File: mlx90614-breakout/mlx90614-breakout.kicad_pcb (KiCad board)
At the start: 2 copper layers, 12.7 x 25.4 mm, 8 parts, among them J1 Conn_01x04_Male, U1 MLX90614

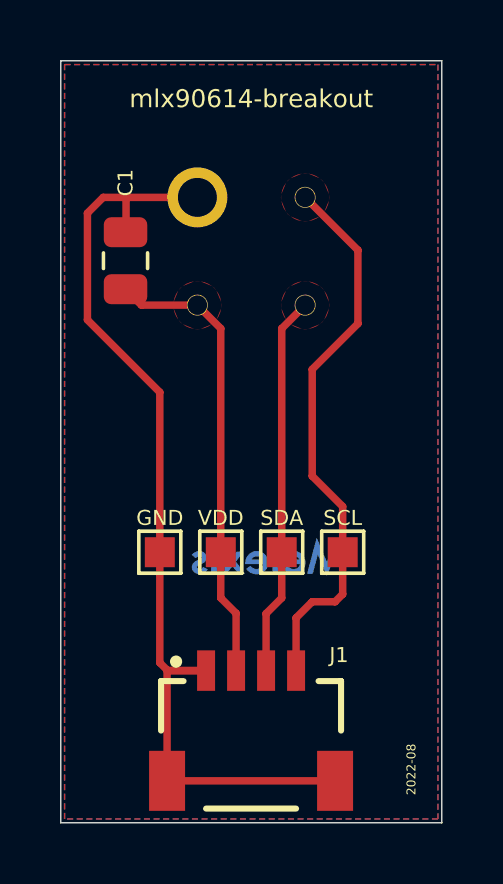
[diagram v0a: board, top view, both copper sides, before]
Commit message: updated breakout boards
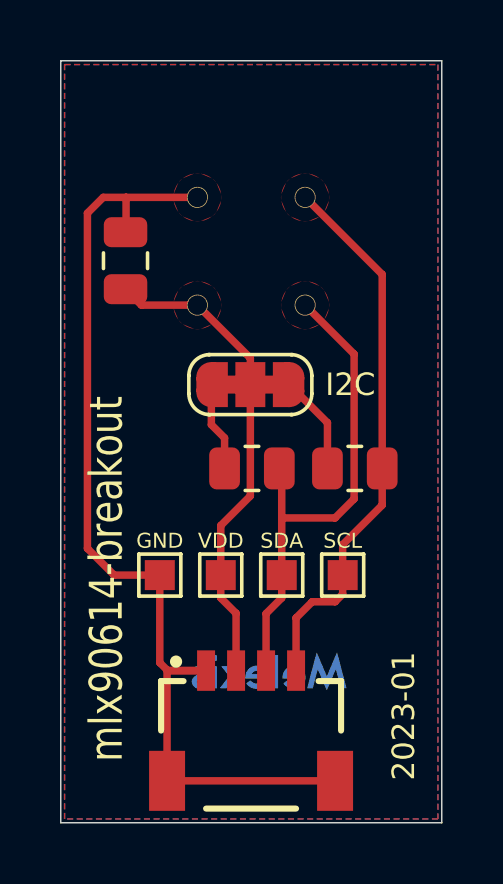
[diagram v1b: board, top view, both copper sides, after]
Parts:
- added I2C: SolderJumper_3_Bridged123, Jumper:SolderJumper-3_P1.3mm_Bridged12_RoundedPad1.0x1.5mm_NumberLabels, F.Cu at (110.9, 68.9)
- added R1: 4K7, Resistor_SMD:R_0805_2012Metric, F.Cu at (114.4, 71.7)
- added R2: 4K7, Resistor_SMD:R_0805_2012Metric, F.Cu at (111.0, 71.7)
- moved G*** 3.82 mm to (110.9, 78.4)
- moved GND 0.76 mm to (107.9, 75.2)
- moved SCL 0.76 mm to (114.0, 75.2)
- moved SDA 0.76 mm to (112.0, 75.2)
- moved VDD 0.76 mm to (109.9, 75.2)
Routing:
- net /SDA: track 12.7 -> 16.8 mm
- net Net-(JP1-Pad3): track 0.00 -> 3.32 mm
- net Net-(JP1-Pad1): track 0.00 -> 2.98 mm
- net /GND: track 33.3 -> 34.2 mm
- net /VDD: track 15.3 -> 16.1 mm
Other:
- board text added: "2023-01"
- board text added: "MLX90614"
- board text removed: "2022-08"
